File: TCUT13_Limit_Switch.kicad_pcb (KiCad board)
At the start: 2 copper layers, 22 x 11.6 mm, 14 parts, among them J1 533980471, Q1 BC847, Q2 BC847, U1 TCUT1300X01

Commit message: [Sudhanshu] Endstop with final Setup
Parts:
- added C1: 0.1uF_0603, morphle_footprints:Cap_0603_1608Metric, F.Cu at (123.0, 88.9)
- added D2: LED_SMD_0603, morphle_footprints:LED_0603_1608Metric, F.Cu at (115.2, 88.4)
- added R8: 1K_0603, morphle_footprints:R_0603_1608Metric, F.Cu at (112.8, 83.2)
- D1: footprint Diode_SMD:D_0402_1005Metric -> morphle_footprints:LED_0603_1608Metric
- J1: value 533980471 -> 5055680471; footprint Molex_1.25_533980471:CON_533980471 -> morphle_footprints:MOLEX_5055680471
- R1, R2, R3, R4, R5, R6, R7: footprint Resistor_SMD:R_0402_1005Metric -> morphle_footprints:R_0603_1608Metric
- moved R4 60.3 mm to (104.2, 84.3), turned to 0 degrees
- moved D1 59.5 mm to (112.1, 88.4)
- moved R3 58.5 mm to (112.9, 90.3)
- moved J1 58.5 mm to (119.4, 84.6), turned to 0 degrees
- moved Q1 58.2 mm to (108.6, 92.6), turned to -90 degrees
- moved Q2 57.5 mm to (109.4, 84.2), turned to -90 degrees
- moved R2 56.3 mm to (112.9, 92.0), turned to 180 degrees
- moved S3 55.2 mm to (106.0, 88.4)
- moved U1 55.2 mm to (106.0, 88.4)
- moved R5 55.1 mm to (104.2, 92.2)
- moved R1 51.4 mm to (112.9, 93.5), turned to 180 degrees
- moved H1 50.7 mm to (119.3, 91.0)
- moved R6 47.6 mm to (112.8, 86.3), turned to 180 degrees
- moved R7 47.6 mm to (112.8, 84.8), turned to 180 degrees
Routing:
- net +3.3V: track 30.9 -> 44.8 mm, vias 2 -> 4
- net /output2: track 23.0 -> 16.3 mm
- net Net-(D2-A): track 0.00 -> 6.24 mm
- net GND: track 7.72 -> 1.65 mm, vias 1 -> 2
- net /Emitter_in2: track 12.9 -> 7.08 mm, vias 2 -> 0
- net /output1: track 11.3 -> 16.1 mm
- net /Emitter_in1: track 5.79 -> 8.17 mm, vias 0 -> 2
- net Net-(R4-Pad2): track 2.75 -> 4.78 mm
- net Net-(D1-A): track 1.20 -> 2.19 mm
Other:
- board size 22 x 11.6 mm -> 22.1 x 12 mm
- board text added: "Morphle_Labs Micro_Endstop_V1"

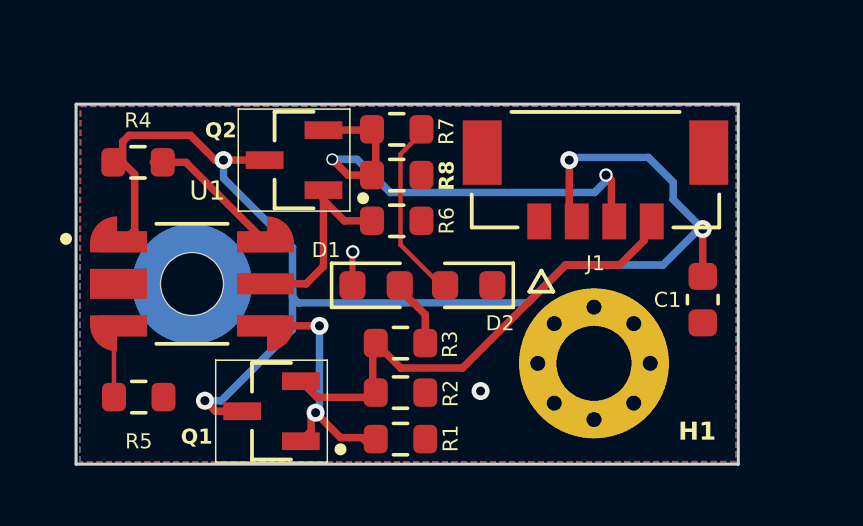
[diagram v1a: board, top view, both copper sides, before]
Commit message: sudhanshu Final PCB with 2 Connector Right angle and upside Connector in a same place
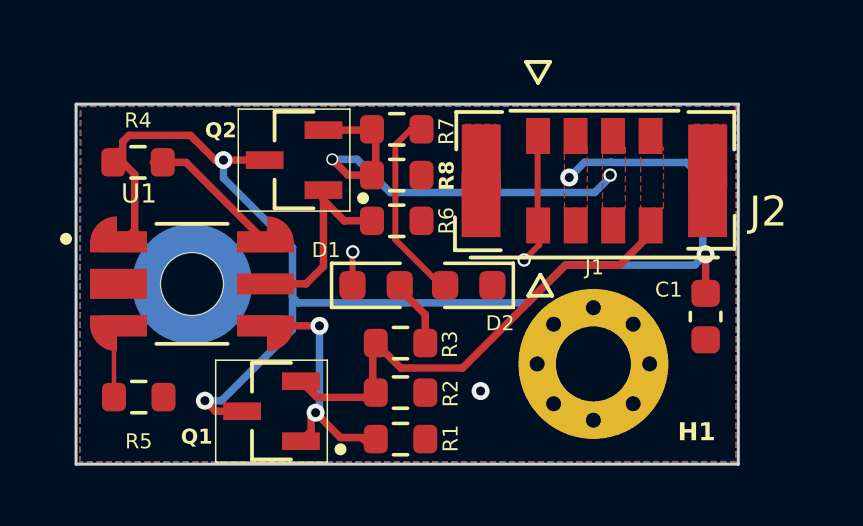
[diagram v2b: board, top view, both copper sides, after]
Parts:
- added J2: 5055670471, molex_1.25_5055670471:MOLEX_5055670471, F.Cu at (119.4, 85.2)
- U1: footprint TCUT13XXX:XDCR_TCUT1300X01 -> TCUT13XX:XDCR_TCUT1300X01
- moved C1 0.57 mm to (123.1, 89.5)
- moved J1 0.14 mm to (119.4, 84.7)
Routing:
- net GND: track 1.65 -> 6.16 mm, vias 2 -> 3
- net /output2: track 16.3 -> 15.1 mm
- added copper zone on F.Cu, net +3.3V
- added copper zone on F.Cu, net /output1
- added copper zone on F.Cu, net /output2
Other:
- board text removed: "Morphle_labs Micro_Limit_switch_V.1"

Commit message: Final PCB Edit
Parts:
- moved Q1 58.8 mm to (163.9, 72.9)
- moved C1 58.8 mm to (178.4, 69.8)
- moved D2 58.8 mm to (170.5, 68.7)
- moved H1 58.8 mm to (174.7, 71.3)
- moved R5 58.8 mm to (159.5, 72.4)
- moved S3 58.8 mm to (161.3, 68.7)
- moved U1 58.8 mm to (161.3, 68.7)
- moved D1 58.8 mm to (167.4, 68.7)
- moved R1 58.8 mm to (168.2, 73.8)
- moved R2 58.8 mm to (168.2, 72.3)
- moved R3 58.8 mm to (168.2, 70.6)
- moved R4 58.8 mm to (159.5, 64.6)
- moved J1 58.6 mm to (174.6, 65.0)
- moved J2 58.6 mm to (174.6, 65.5)
- moved R6 58.5 mm to (167.9, 66.6)
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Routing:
- net GND: track 6.16 -> 0.61 mm
- net +3.3V: track 44.4 -> 43.7 mm
- net /Emitter_in2: track 7.08 -> 6.42 mm
- net /output2: track 15.1 -> 14.5 mm
- net /Emitter_in1: track 8.17 -> 8.68 mm
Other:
- board size 22.1 x 12 mm -> 22 x 12 mm

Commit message: [sudhasnhu] added Some Change New Repo
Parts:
- removed Q1, Q2: BC847, morphle_footprints:BC847
- added U2: BC857A, bc857:SOT95P240X110-3N, F.Cu at (164.5, 72.9)
- added U3: BC857A, bc857:SOT95P240X110-3N, F.Cu at (164.2, 64.5)
- H1: footprint MountingHole:MountingHole_2.5mm_Pad_Via -> MountingHole:MountingHole_2.7mm_M2.5_Pad_Via
- moved H1 0.21 mm to (174.8, 71.5)
- moved C1 0.13 mm to (178.6, 69.8)
- moved U1 0.07 mm to (161.2, 68.7)
- moved S3 0.07 mm to (161.2, 68.7)
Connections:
- J1 pad 2: +3.3V -> /output1
- J1 pad 4: /output1 -> +3.3V
- J2 pad 2: +3.3V -> /output1
- J2 pad 4: /output1 -> +3.3V
- R1 pad 1: GND -> /Emitter_in1
- R1 pad 2: /Emitter_in1 -> Net-(U2-B)
- R2 pad 1: GND -> Net-(U2-B)
- R2 pad 2: /output1 -> +3.3V
- R6 pad 1: GND -> +3.3V
- R6 pad 2: /Emitter_in2 -> Net-(U3-B)
- R7 pad 1: GND -> /Emitter_in2
- R7 pad 2: /output2 -> Net-(U3-B)
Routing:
- net GND: track 0.61 -> 5.25 mm, vias 3 -> 1
- net Net-(U2-B): track 0.00 -> 4.20 mm
- net +3.3V: track 43.7 -> 47.4 mm, vias 4 -> 2
- net Net-(U3-B): track 0.00 -> 3.52 mm
- net /Emitter_in1: track 8.68 -> 11.7 mm
- net /Emitter_in2: track 6.42 -> 8.34 mm, vias 0 -> 2
- net /output2: track 14.5 -> 13.1 mm
- net /output1: track 16.0 -> 16.4 mm, vias 0 -> 2
